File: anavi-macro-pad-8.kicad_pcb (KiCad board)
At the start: 2 copper layers, 135 x 47.1 mm, 48 parts, among them J1 USB_B_Micro, J2 Conn_01x04_Female, J3 Conn_01x03_Male, J4 Conn_01x03_Male, J5 AVR-ISP-6, Q1 Q_NPN_BEC, SW1 SW_DIP_x01, SW2 SW_DIP_x01, SW3 SW_DIP_x01, SW4 SW_DIP_x01, SW5 SW_DIP_x01, SW6 SW_DIP_x01, SW7 SW_DIP_x01, SW8 SW_DIP_x01, SW9 SW_DIP_x01, U1 ATmega32U4-AU, Y1 Crystal

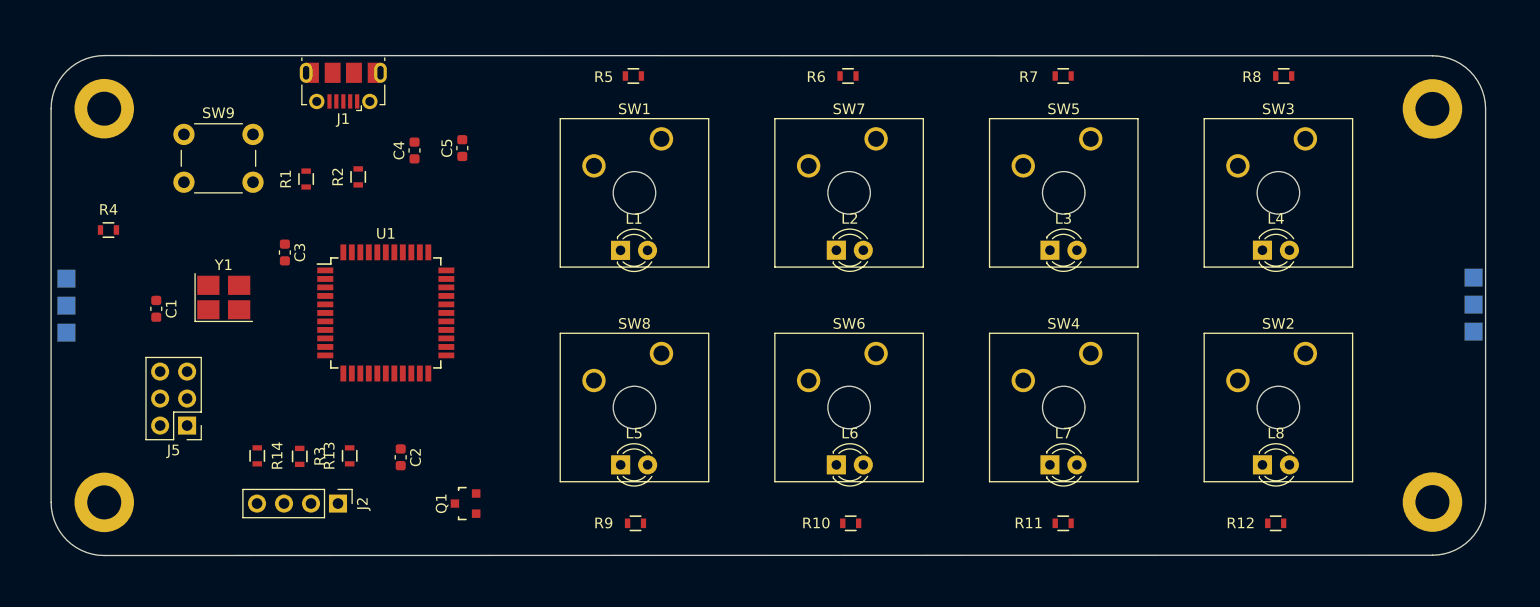
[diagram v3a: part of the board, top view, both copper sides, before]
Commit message: anavi-macro-pad-8.kicad_pcb: Initial routing
Work in progress on the routing of the PCB

Signed-off-by: Leon Anavi <leon@anavi.org>
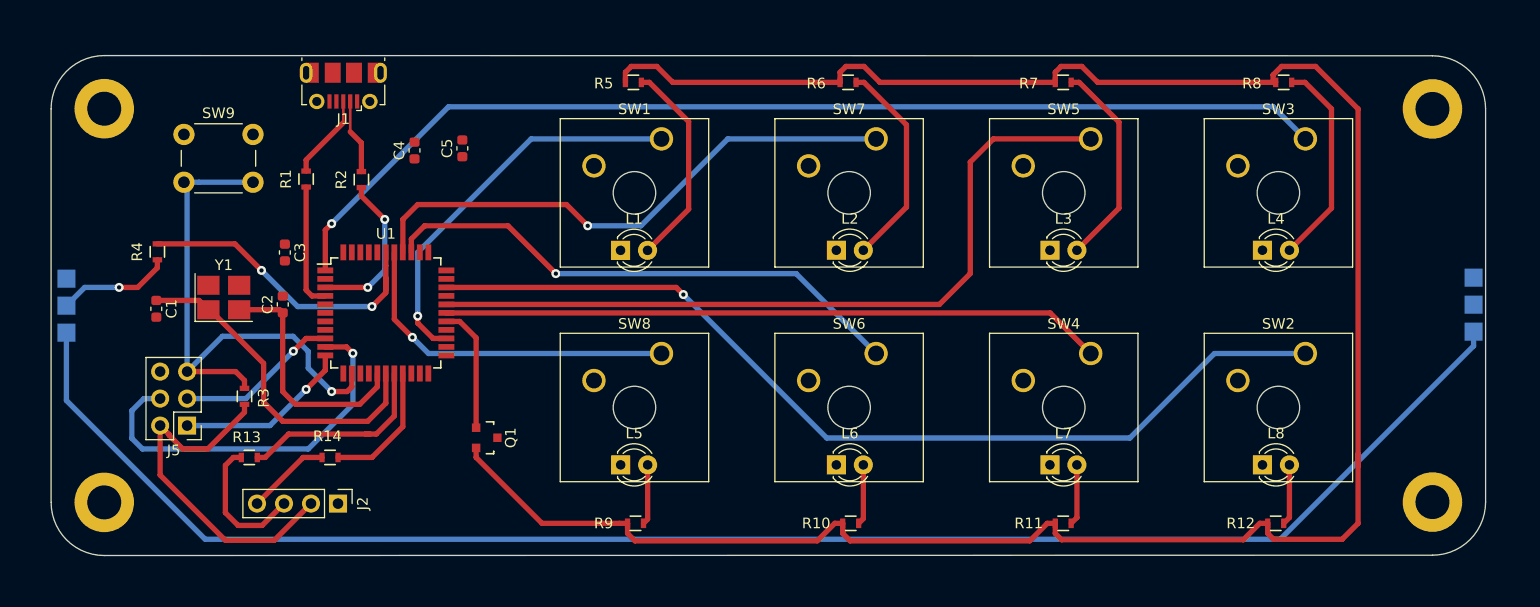
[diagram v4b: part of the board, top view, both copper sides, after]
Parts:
- moved C2 18.2 mm to (66.8, 78.4), turned to 90 degrees
- moved R13 9.45 mm to (63.6, 92.8), turned to 0 degrees
- moved R3 7.68 mm to (63.2, 87.0)
- moved R14 6.85 mm to (71.2, 92.8), turned to 0 degrees
- moved Q1 6.51 mm to (86.0, 91.0), turned to 270 degrees
- moved R4 5.04 mm to (55.0, 73.5), turned to 90 degrees
- moved R5 0.60 mm to (99.8, 57.5)
- moved R6 0.60 mm to (120.0, 57.5)
- moved R7 0.60 mm to (140.2, 57.5)
- moved R8 0.60 mm to (161.0, 57.5)
- moved R2 0.39 mm to (74.2, 66.7)
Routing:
- net Net-(Q1-Pad2): track 0.00 -> 211.3 mm
- net +5V: track 0.00 -> 187.1 mm
- net Net-(SW3-Pad1): track 0.00 -> 102.1 mm, vias 0 -> 1
- net Net-(SW2-Pad1): track 0.00 -> 90.0 mm, vias 0 -> 1
- net Net-(SW5-Pad1): track 0.00 -> 73.2 mm
- net Net-(SW4-Pad1): track 0.00 -> 62.2 mm
- net Net-(SW7-Pad1): track 0.00 -> 52.4 mm, vias 0 -> 1
- net Net-(J5-Pad5): track 0.00 -> 52.3 mm, vias 0 -> 1
- net Net-(SW6-Pad1): track 0.00 -> 50.5 mm, vias 0 -> 1
- net Net-(SW1-Pad1): track 0.00 -> 37.3 mm, vias 0 -> 1
- net Net-(J5-Pad4): track 0.00 -> 36.3 mm, vias 0 -> 1
- net Net-(SW8-Pad1): track 0.00 -> 32.8 mm, vias 0 -> 1
- net Net-(C1-Pad1): track 0.00 -> 32.0 mm
- net Net-(R4-Pad2): track 0.00 -> 29.5 mm, vias 0 -> 2
- net Net-(C2-Pad1): track 0.00 -> 23.0 mm
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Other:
- net class Default: clearance 0.2 -> 0.254; trace_width 0.25 -> 0.5; via_dia 0.8 -> 0.85
- net class usb added: clearance 0.254, trace_width 0.254, via_dia 0.85, via_drill 0.4
- net class vcc added: clearance 0.254, trace_width 1.5, via_dia 0.85, via_drill 0.4
- rule pad_to_mask_clearance: 0.051 -> 0.2
- rule trace_clearance: 0.2 -> 0.254

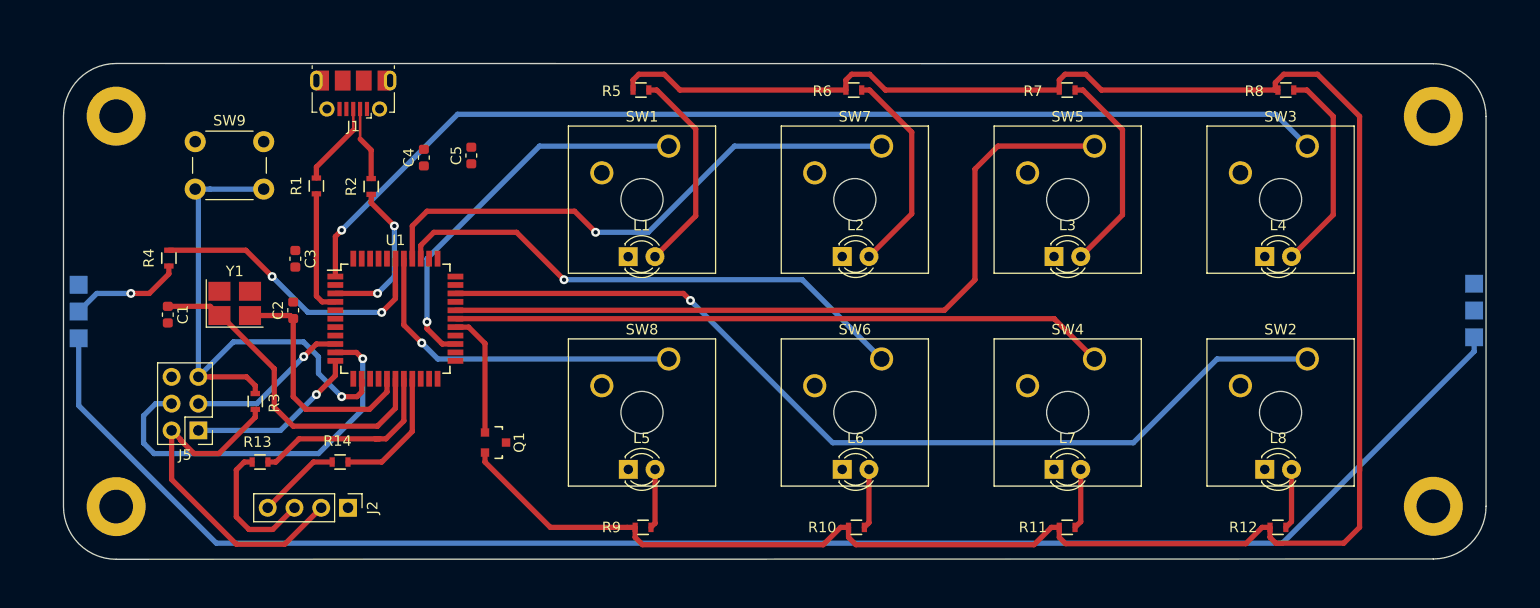
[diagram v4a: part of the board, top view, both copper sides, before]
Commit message: anavi-macro-pad-8: Routing with Schottky diode
Add appropriate footprint for Schottky diode and complete the
routing of the PCB.

Signed-off-by: Leon Anavi <leon@anavi.org>
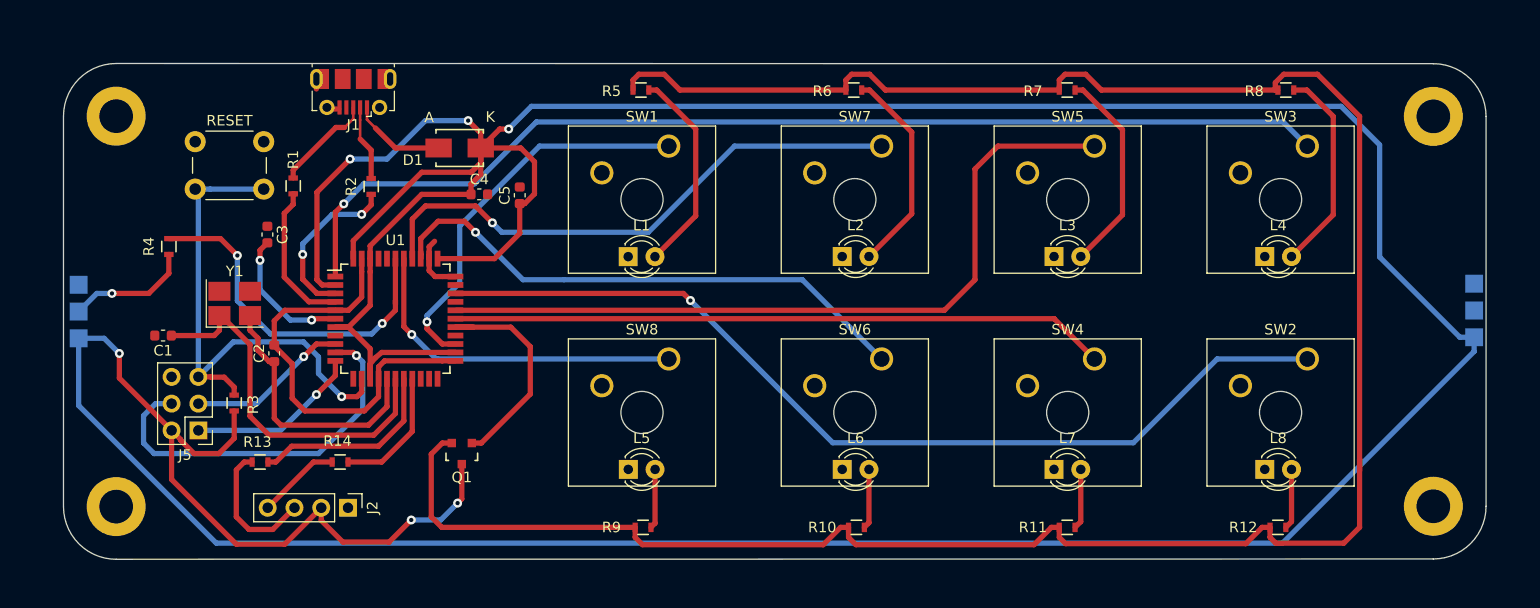
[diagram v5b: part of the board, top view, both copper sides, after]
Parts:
- added D1: 1N5819, Diodes_SMD:SMA_Standard, F.Cu at (82.6, 63.0)
- moved C4 6.31 mm to (84.5, 67.4), turned to 0 degrees
- moved C5 5.95 mm to (88.3, 67.5)
- moved C2 4.47 mm to (65.0, 82.5)
- moved C3 3.51 mm to (64.3, 71.2)
- moved Q1 3.37 mm to (82.8, 92.0), turned to 180 degrees
- moved R1 2.20 mm to (66.8, 66.6)
- moved C1 2.04 mm to (54.5, 80.8), turned to 180 degrees
- moved R3 2.01 mm to (61.2, 87.2)
- moved R4 1.10 mm to (55.0, 72.3)
- moved J1 0.15 mm to (72.5, 57.7)
- renumbered SW9 to RESET
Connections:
- J1 pad 1: (no net) -> Net-(D1-Pad2)
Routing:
- net +5V: track 187.1 -> 447.7 mm, vias 0 -> 6
- net GND: track 0.00 -> 48.6 mm
- net Net-(C3-Pad2): track 0.00 -> 13.1 mm, vias 0 -> 2
- net Net-(Q1-Pad2): track 211.3 -> 221.7 mm
- net /BACKLIT: track 11.9 -> 21.5 mm
- net Net-(D1-Pad2): track 0.00 -> 9.27 mm
- net Net-(R4-Pad2): track 29.5 -> 33.9 mm
- net Net-(C1-Pad1): track 32.0 -> 35.7 mm
- net Net-(R1-Pad1): track 11.7 -> 14.3 mm
- net Net-(C2-Pad1): track 23.0 -> 25.3 mm
- net Net-(J5-Pad5): track 52.3 -> 50.4 mm
- net Net-(SW6-Pad1): track 50.5 -> 52.2 mm
- net Net-(J1-Pad3): track 8.00 -> 9.55 mm
- net Net-(J3-Pad2): track 10.8 -> 11.9 mm
- net Net-(R2-Pad1): track 15.0 -> 16.0 mm
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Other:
- outline, holes or cut-outs redrawn

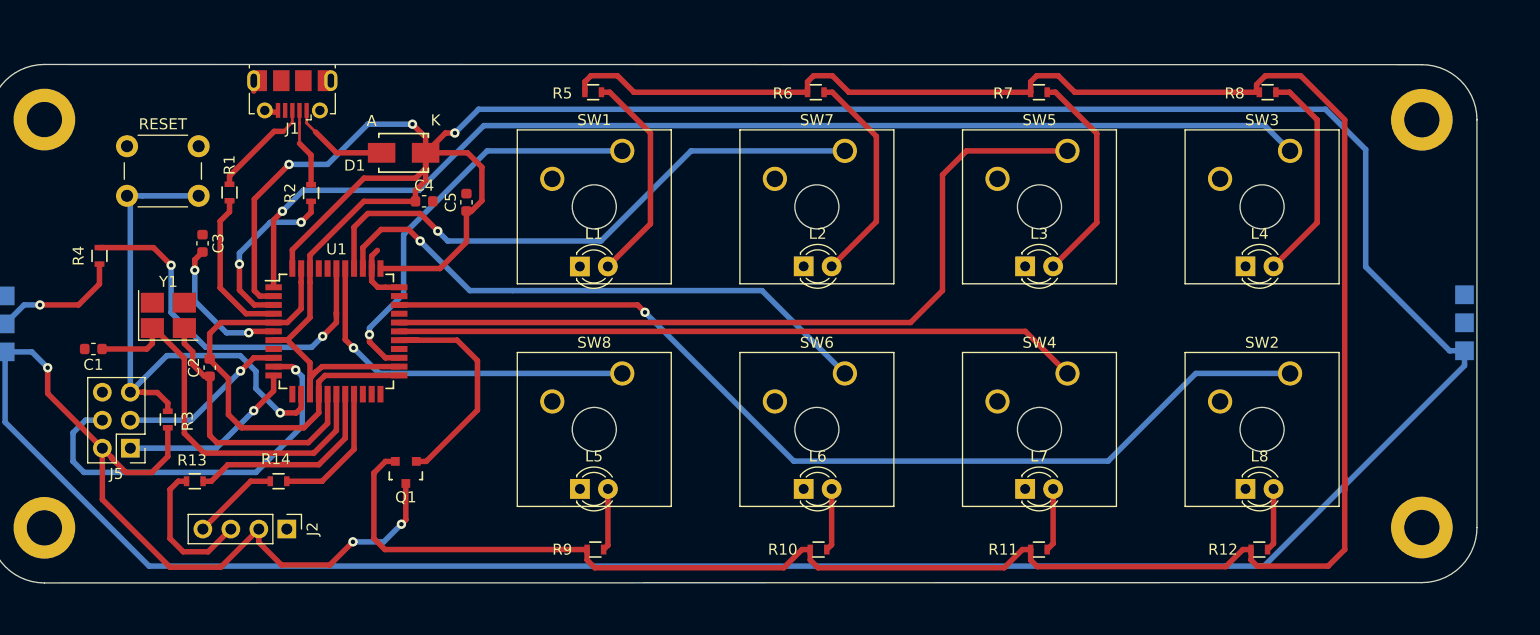
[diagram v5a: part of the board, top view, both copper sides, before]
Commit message: anavi-macro-pad-8.kicad_pcb: Add logo and labels
Add logo and labels on the PCB.

Signed-off-by: Leon Anavi <leon@anavi.org>
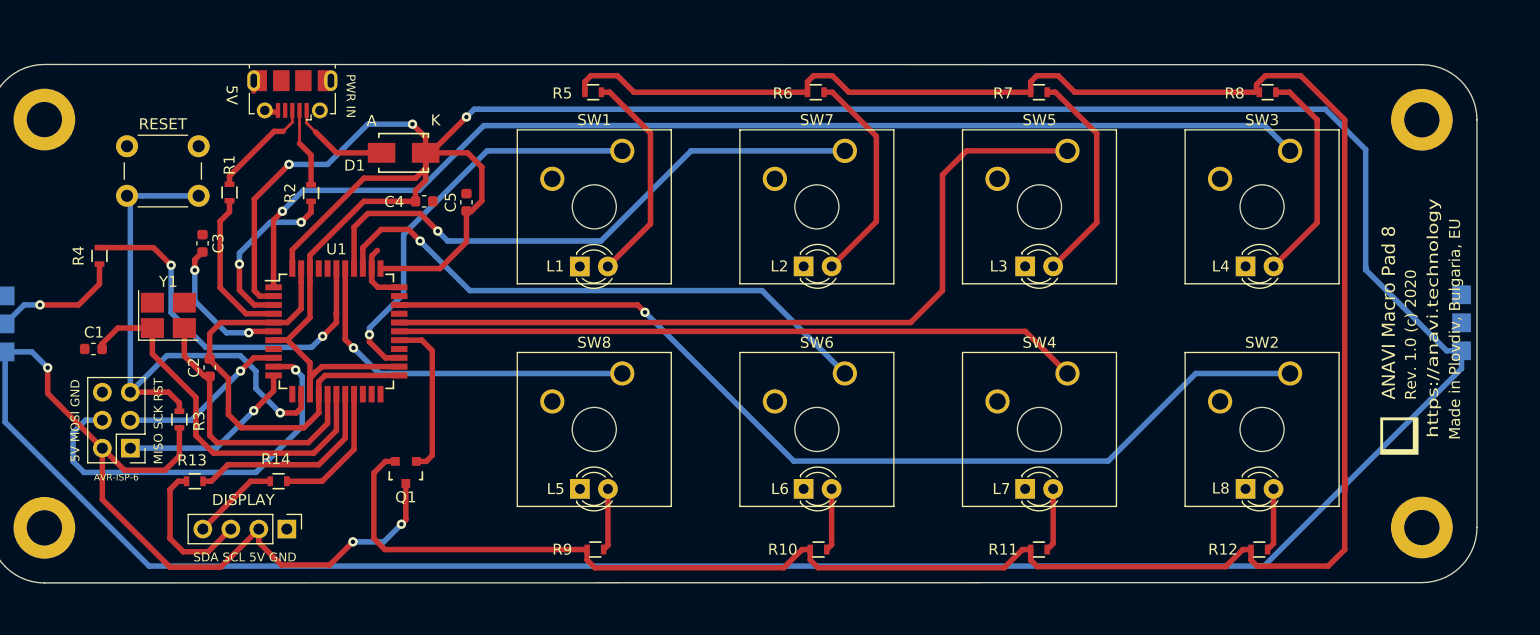
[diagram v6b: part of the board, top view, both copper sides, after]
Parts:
- added G***: LOGO, anavi-macro-pad-8:anavi-logo, F.Cu at (173.0, 88.7)
- moved R3 1.05 mm to (62.2, 87.2)
- moved J4 0.27 mm to (178.6, 81.0)
- renumbered J5 to AVR-ISP-6, J2 to DISPLAY
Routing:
- net /BACKLIT: track 21.5 -> 14.6 mm
- net Net-(J5-Pad5): track 50.4 -> 51.4 mm
- net Net-(C1-Pad1): track 35.7 -> 34.7 mm
- net +5V: track 447.7 -> 448.4 mm
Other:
- board text added: "5V"
- board text added: "5V MOSI GND"
- board text added: "ANAVI Macro Pad 8"
- board text added: "MISO SCK RST"
- board text added: "Made in Plovdiv, Bulgaria, EU"
- board text added: "PWR IN"
- board text added: "Rev. 1.0 (c) 2020"
- board text added: "SDA SCL 5V GND"
- board text added: "https://anavi.technology"

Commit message: Minor improvements
Signed-off-by: Leon Anavi <leon@anavi.org>
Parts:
- Q1: value Q_NPN_BEC -> BC817
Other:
- net class Default: clearance 0.254 -> 0.25
- rule trace_clearance: 0.254 -> 0.25
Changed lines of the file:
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@@
     (user_trace_width 0.254)
     (user_trace_width 0.5)
-    (trace_clearance 0.254)
+    (trace_clearance 0.25)
     (zone_clearance 0.508)
     (zone_45_only no)
@@
   (net 38 "Net-(D1-Pad2)")
   (net_class Default "This is the default net class."
-    (clearance 0.254)
+    (clearance 0.25)
     (trace_width 0.5)
     (via_dia 0.85)
@@
     (tags "resistor 0603")
     (attr smd)
-    (fp_text reference R4 (at 0 -1.9 90) (layer F.SilkS)
+    (fp_text reference R4 (at 0 -1.7 90) (layer F.SilkS)
       (effects (font (size 1 1) (thickness 0.15)))
     )
@@
     (tags capacitor)
     (attr smd)
-    (fp_text reference C3 (at 0 -1.43 90) (layer F.SilkS)
+    (fp_text reference C3 (at -0.0125 -1.55 90) (layer F.SilkS)
       (effects (font (size 1 1) (thickness 0.15)))
     )
@@
     (tags SOT-23)
     (attr smd)
-    (fp_text reference Q1 (at 0 -2.25) (layer F.SilkS)
-      (effects (font (size 1 1) (thickness 0.15)))
-    )
-    (fp_text value Q_NPN_BEC (at 0 2.3) (layer F.Fab)
+    (fp_text reference Q1 (at 0 -2.39822) (layer F.SilkS)
+      (effects (font (size 1 1) (thickness 0.15)))
+    )
+    (fp_text value BC817 (at 0 2.40178) (layer F.Fab)
       (effects (font (size 1 1) (thickness 0.15)))
     )
@@
     (tags "resistor 0603")
     (attr smd)
-    (fp_text reference R1 (at 2.5 0 90) (layer F.SilkS)
-      (effects (font (size 1 1) (thickness 0.15)))
-    )
-    (fp_text value 20R (at 0 1.9 90) (layer F.Fab)
+    (fp_text reference R1 (at 0 1.7 90) (layer F.SilkS)
+      (effects (font (size 1 1) (thickness 0.15)))
+    )
+    (fp_text value 20R (at 3 0 90) (layer F.Fab)
       (effects (font (size 1 1) (thickness 0.15)))
     )
@@
     (tags "resistor 0603")
     (attr smd)
-    (fp_text reference R2 (at 0 -1.9 90) (layer F.SilkS)
+    (fp_text reference R2 (at 0 -1.6 90) (layer F.SilkS)
       (effects (font (size 1 1) (thickness 0.15)))
     )
@@
       (effects (font (size 1 1) (thickness 0.15)))
     )
-    (fp_text value SW_DIP_x01 (at -2.54 12.954) (layer F.Fab)
+    (fp_text value SW_DIP_x01 (at -2.54 12.954) (layer F.Fab) hide
       (effects (font (size 1 1) (thickness 0.15)))
     )
@@
     (descr "Through hole straight pin header, 2x03, 2.54mm pitch, double rows")
     (tags "Through hole pin header THT 2x03 2.54mm double row")
-    (fp_text reference AVR-ISP-6 (at 1.27 -2.65) (layer F.SilkS)
-      (effects (font (size 0.6 0.6) (thickness 0.1)))
+    (fp_text reference AVR-ISP-6 (at 1.3 -2.65) (layer F.SilkS)
+      (effects (font (size 0.8 0.7) (thickness 0.1)))
     )
     (fp_text value AVR-ISP-6 (at 3.4 -3.6 180) (layer F.Fab) hide
@@
     (descr "tactile push button, 6x6mm e.g. PHAP33xx series, height=4.3mm")
     (tags "tact sw push 6mm")
-    (fp_text reference RESET (at 3.25 -2) (layer F.SilkS)
+    (fp_text reference RESET (at 3.25 -2.1) (layer F.SilkS)
       (effects (font (size 1 1) (thickness 0.15)))
     )
@@
     (tags "Diode SMA")
     (attr smd)
-    (fp_text reference D1 (at 4.44898 -1.15) (layer F.SilkS)
+    (fp_text reference D1 (at 4.59898 -1.15) (layer F.SilkS)
       (effects (font (size 1 1) (thickness 0.15)))
     )
@@
   )
   (gr_text 5V (at 67 57.75 270) (layer F.SilkS)
-    (effects (font (size 1 1) (thickness 0.1)))
+    (effects (font (size 1 1) (thickness 0.15)))
   )
   (gr_text "PWR IN" (at 77.8 57.85 270) (layer F.SilkS)
